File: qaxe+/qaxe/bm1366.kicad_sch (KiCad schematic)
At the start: 95 parts, among them J2 Conn_01x06, Q7 BSS138, U10 +0V8, U11 +0V8, U12 +0V8, U13 +0V8, U14 +0V8, U15 +0V8, U16 +0V8, U17 +0V8, U18 +0V8, U19 BM1368_mode1, U20 BM1368_mode1, U21 +0V8, U22 +0V8, U23 +0V8, U24 +0V8, U25 BM1368_mode1, U26 BM1368_mode1, U27 +0V8, U28 +0V8, U29 TXU0101, U31 +0V8, U34 +0V8, U38 TXU0101, U8 25MHz, U9 +0V8

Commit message: qaxe+
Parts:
- added R44, R45, R46, R47: 1k, Resistor_SMD:R_0805_2012Metric, symbol Device:R
- U19, U20, U25, U26: footprint myfootprints:BM1368-smaller -> bitaxe:BM1368
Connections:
- net GND: now also R44.2, R45.2, R46.2, R47.2
- net at U25.11 (?): now also R47.1
- net at U26.11 (?): now also R45.1
- net at U19.11 (?): now also R46.1
- net at U20.11 (?): now also R44.1
- no-connect marks 28 -> 24
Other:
- moved on the sheet: R20, R21

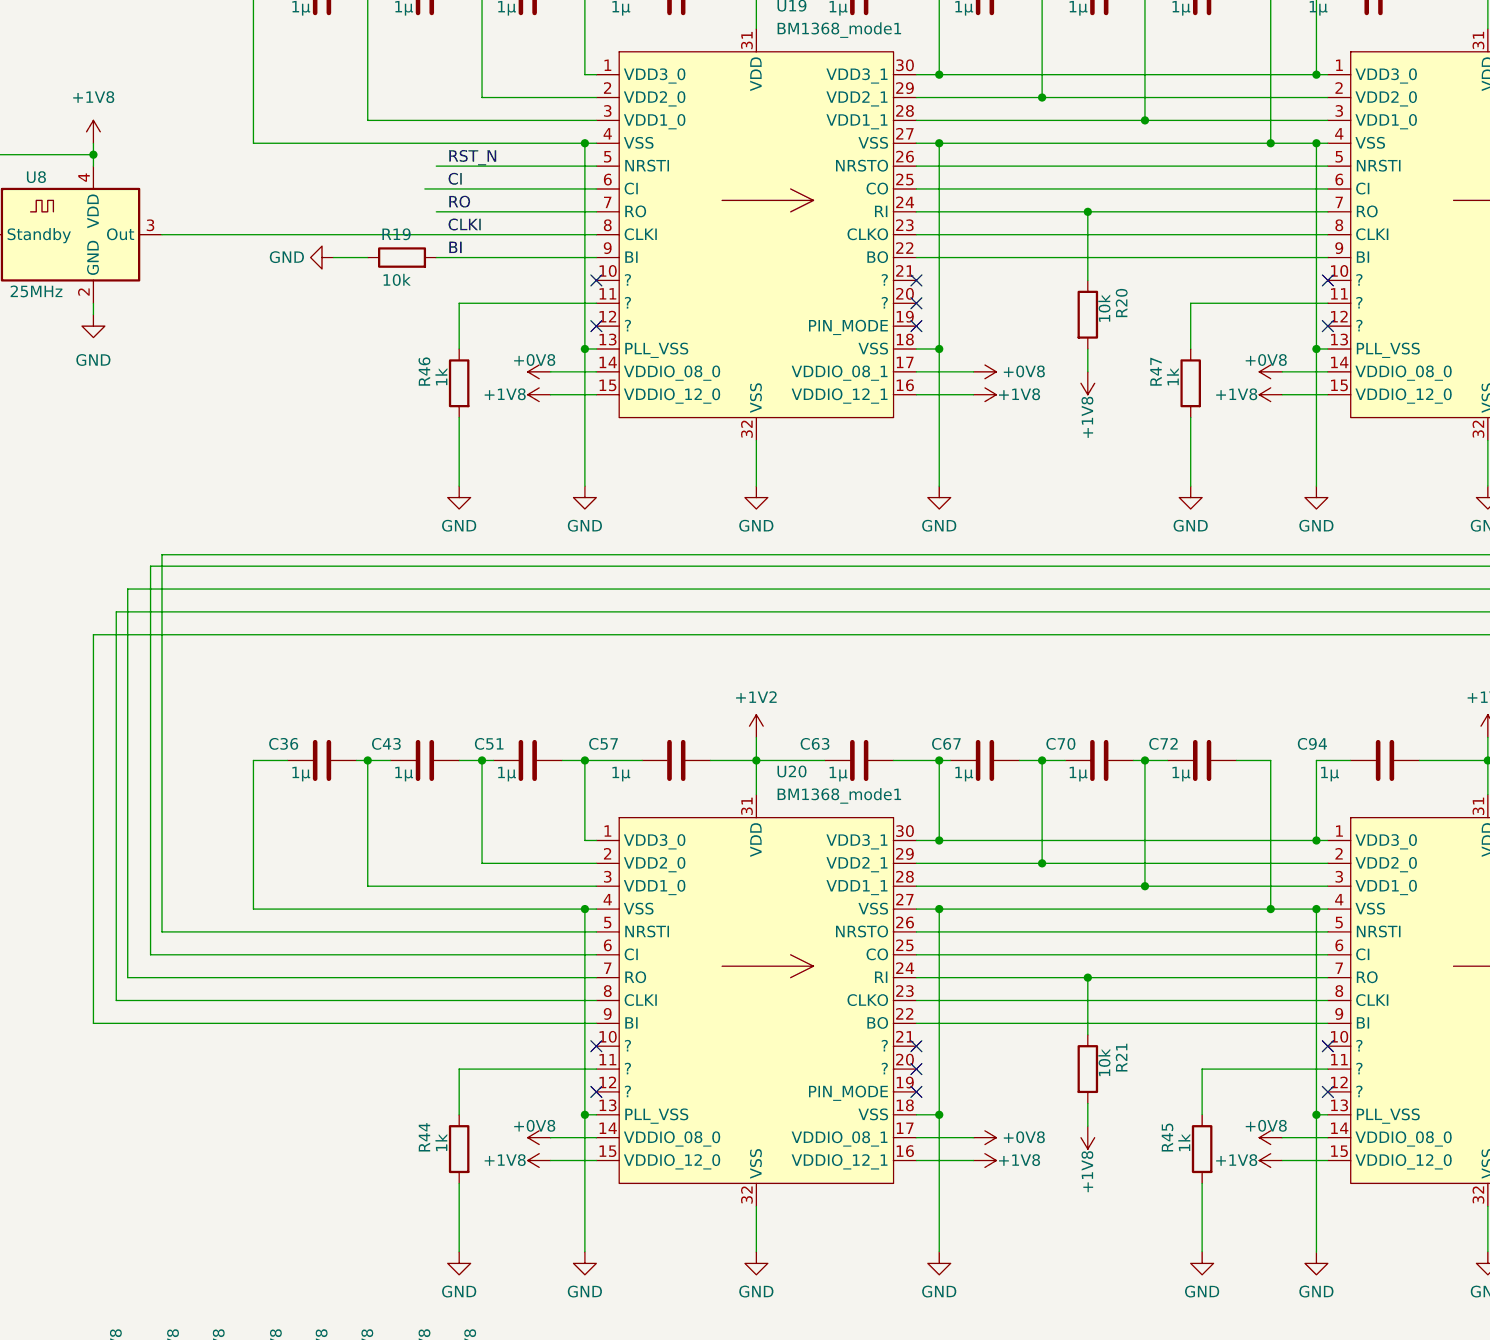
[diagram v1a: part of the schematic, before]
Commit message: rev4.1 qaxe+ (added pull downs on NRSTI)
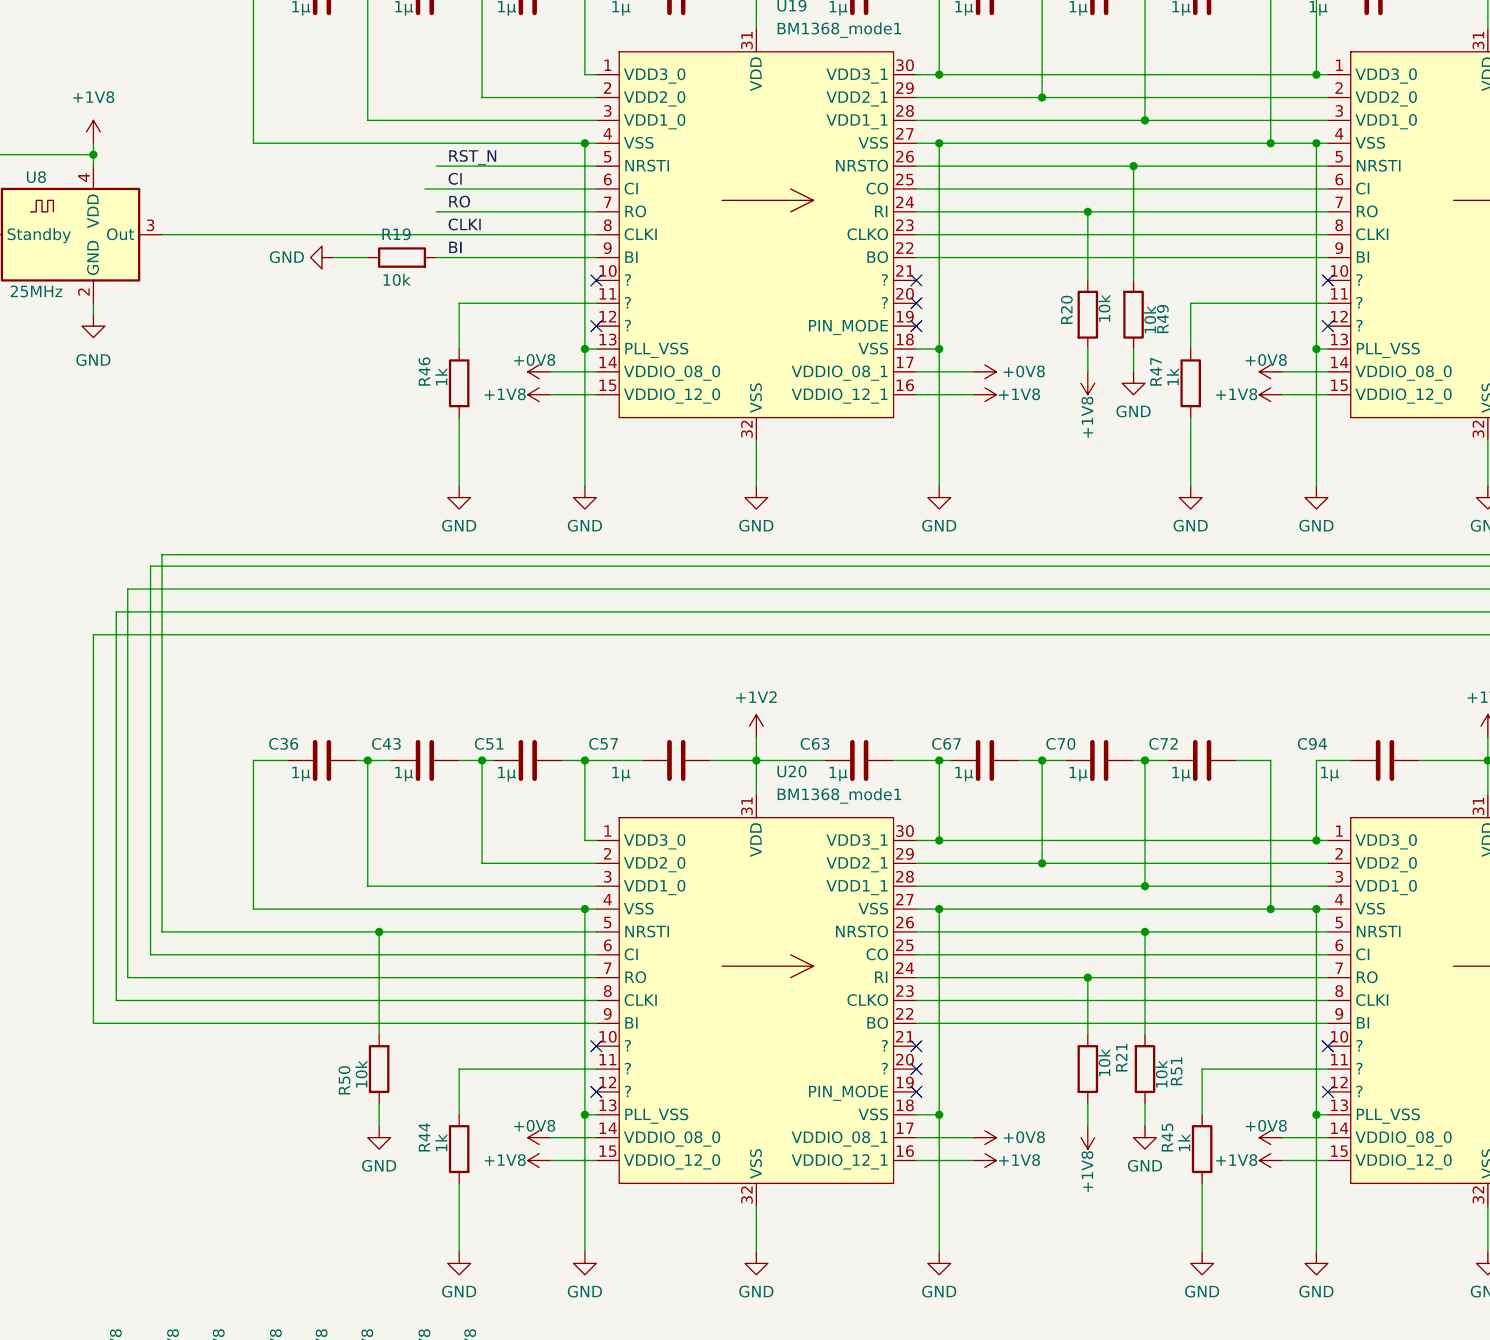
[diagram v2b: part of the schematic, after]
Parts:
- added R49, R50, R51: 10k, Resistor_SMD:R_0805_2012Metric, symbol Device:R
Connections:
- net GND: now also R49.1, R50.1, R51.1
- net at U20.5 (NRSTI), U25.26 (NRSTO): now also R50.2
- net at U19.26 (NRSTO), U25.5 (NRSTI): now also R49.2
- net at U20.26 (NRSTO), U26.5 (NRSTI): now also R51.2
